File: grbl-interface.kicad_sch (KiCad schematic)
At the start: 12 parts, among them U6 USBLC6-2SC6, U7 ADUM4160, U8 ATmega16U2-A, U9 ATmega328P-A, Y1 Crystal_GND24

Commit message: GRBL PCB controller work
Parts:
- removed D10, D9: Znr, symbol Device:D_Zener
- removed D8: D_Zener, symbol Device:D_Zener
- added C13, C14: 22p, Capacitor_SMD:C_0402_1005Metric_Pad0.74x0.62mm_HandSolder, symbol Device:C
- added C15: 1u, Capacitor_SMD:C_0603_1608Metric, symbol Device:C
- added C16, C18, C19, C20, C21, C24, C25, C26: 100n, Capacitor_SMD:C_0603_1608Metric, symbol Device:C
- added C27: 22u TANT, Capacitor_SMD:C_1206_3216Metric, symbol Device:C_Polarized_US
- added C28: TBD_SPACER (DNI), symbol Device:C
- added D10, D9: YELLOW, -Project:LED_0402_DOT, symbol Device:LED
- added D11, D8: CD1206-S01575, -Project:D_SOD-523_DOT, symbol Device:D
- added F1: TBU-CA065-500-WH, Fuse:Fuse_Bourns_TBU-CA, symbol Power_Protection:TBU-CA065-500-WH
- added J21: USB_B_Mini, Connector_USB:USB_Mini-B_Wuerth_65100516121_Horizontal, symbol Connector:USB_B_Mini
- added J22: uISP, -Project:ISP_SMD_100mil, symbol Connector_Generic:Conn_02x03_Odd_Even
- added J23: ISP, -Project:ISP_SMD_100mil, symbol Connector_Generic:Conn_02x03_Odd_Even
- added L2: CG0603MLC-05E, symbol Device:L
- added L3: 10uH, symbol Device:L
- added R21: 1M, symbol Device:R
- added R23, R30: 10K, symbol Device:R
- added R25, R26, R27, R28, R29: 1K, symbol Device:R
- added SW3: RESET, symbol Switch:SW_Push
- added Y1: 16MHz, symbol Device:Crystal_GND24
- C17: renamed from C13; value C -> 100n; footprint (none) -> Capacitor_SMD:C_0603_1608Metric
- C22: renamed from C14; value C -> 22p; footprint (none) -> Capacitor_SMD:C_0402_1005Metric_Pad0.74x0.62mm_HandSolder
- C23: renamed from C15; value C -> 22p; footprint (none) -> Capacitor_SMD:C_0402_1005Metric_Pad0.74x0.62mm_HandSolder
- U9: value ATmega328P-A -> ATmega328P-AU
- Y2: renamed from Y1; value Crystal_GND24 -> CSTCE16M0V53-R0 16MHZ
- renumbered R21 to R24, U8 to U7, U7 to U8
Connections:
- net GND3 is gone; now on net uGND: C17.2, R24.1, U8.2 (GND1), U8.8 (GND1)
- net +5VA: now also U7.31 (UVCC), U7.32 (AVCC), U7.4 (VCC), U8.12 (PIN), U8.13 (SPD), U8.14 (VDD2), C16.2, C21.2, C24.2, C25.2, C27.1, D11.1 (K), D8.1 (K), J22.2 (Pin_2), J23.2 (Pin_2), L3.1, R23.1, R28.1, R29.1, R30.1; no longer U9.18 (AVCC)
- net GND1: no longer U9.21 (GND), U9.3 (GND), U9.5 (GND), Y2.4
- net P12_IN: now also J23.1 (Pin_1)
- net P16_OUT: now also J23.3 (Pin_3)
- net P17_OUT: now also J23.4 (Pin_4)
- net RX: now also R27.1
- net TX: now also R26.1
- net uD-: now reaches U6.1 (I/O1)
- net uD-: now also J21.2 (D-)
- net uGND: now reaches U6.2 (GND)
- net uGND: now also C18.1, J21.5 (GND), L2.2
- net uD+: now reaches U6.3 (I/O2)
- net uD+: now also J21.3 (D+)
- net at U6.4 (I/O2): now also U8.7 (UD+)
- net at U6.5 (VBUS): now also C17.1, R24.2, U8.3 (VDD1), U8.4 (PDEN), U8.5 (SPU), F1.3
- net at U6.6 (I/O1): now also U8.6 (UD-)
- net RESET: now reaches U9.29 (~{RESET}/PC6)
- net RESET: now also C20.2, D11.2 (A), J23.5 (Pin_5), R30.2, SW3.2
- net at U7.1 (XTAL1): now also C13.1, R21.2, Y1.1
- net RX_LED: now reaches U7.10 (PD4)
- net RX_LED: now also D9.1 (K)
- net TX_LED: now reaches U7.11 (PD5)
- net TX_LED: now also D10.1 (K)
- net DTR: now reaches U7.13 (~{HWB}/PD7)
- net DTR: now also C20.1, R25.1
- net uSCK: now reaches U7.15 (PB1)
- net uSCK: now also J22.3 (Pin_3)
- net uMOSI: now reaches U7.16 (PB2)
- net uMOSI: now also J22.4 (Pin_4)
- net uMISO: now reaches U7.17 (PB3)
- net uMISO: now also J22.1 (Pin_1)
- net at U7.2 (PC0/XTAL2): now also C14.2, R21.1, Y1.3
- net uRESET: now reaches U7.24 (PC1/~{RESET})
- net uRESET: now also D8.2 (A), J22.5 (Pin_5), R23.2
- net at U7.27 (UCAP): now also C15.1
- net GND: now reaches U7.28 (UGND)
- net GND: now also U7.3 (GND), U8.15 (GND2), U8.9 (GND2), U9.21 (GND), U9.3 (GND), U9.5 (GND), Y2.4, C13.2, C14.1, C15.2, C16.1, C19.1, C21.1, C24.1, C25.1, C26.1, C27.2, J22.6 (Pin_6), J23.6 (Pin_6), R25.2, SW3.1, Y1.2, Y1.4
- net D+: now reaches U7.29 (D+)
- net D+: now also U8.10 (DD+)
- net D-: now reaches U7.30 (D-)
- net D-: now also U8.11 (DD-)
- net uRX: now reaches U7.8 (PD2)
- net uRX: now also R26.2
- net uTX: now reaches U7.9 (PD3)
- net uTX: now also R27.2
- net at U8.1 (VBUS1): now also C18.2, C28.2
- net at U8.16 (VBUS2): now also C19.2, C28.1
- new net: C26.2, L3.2, U9.18 (AVCC)
- new net: D9.2 (A), R28.2
- new net: J21.SH (Shield), L2.1
- new net: D10.2 (A), R29.2
- new net VBUS: F1.1, J21.1 (VBUS)
- no-connect marks 3 -> 19
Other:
- moved on the sheet: C17, C22, C23, R24, U6, U7, U8, U9, Y2

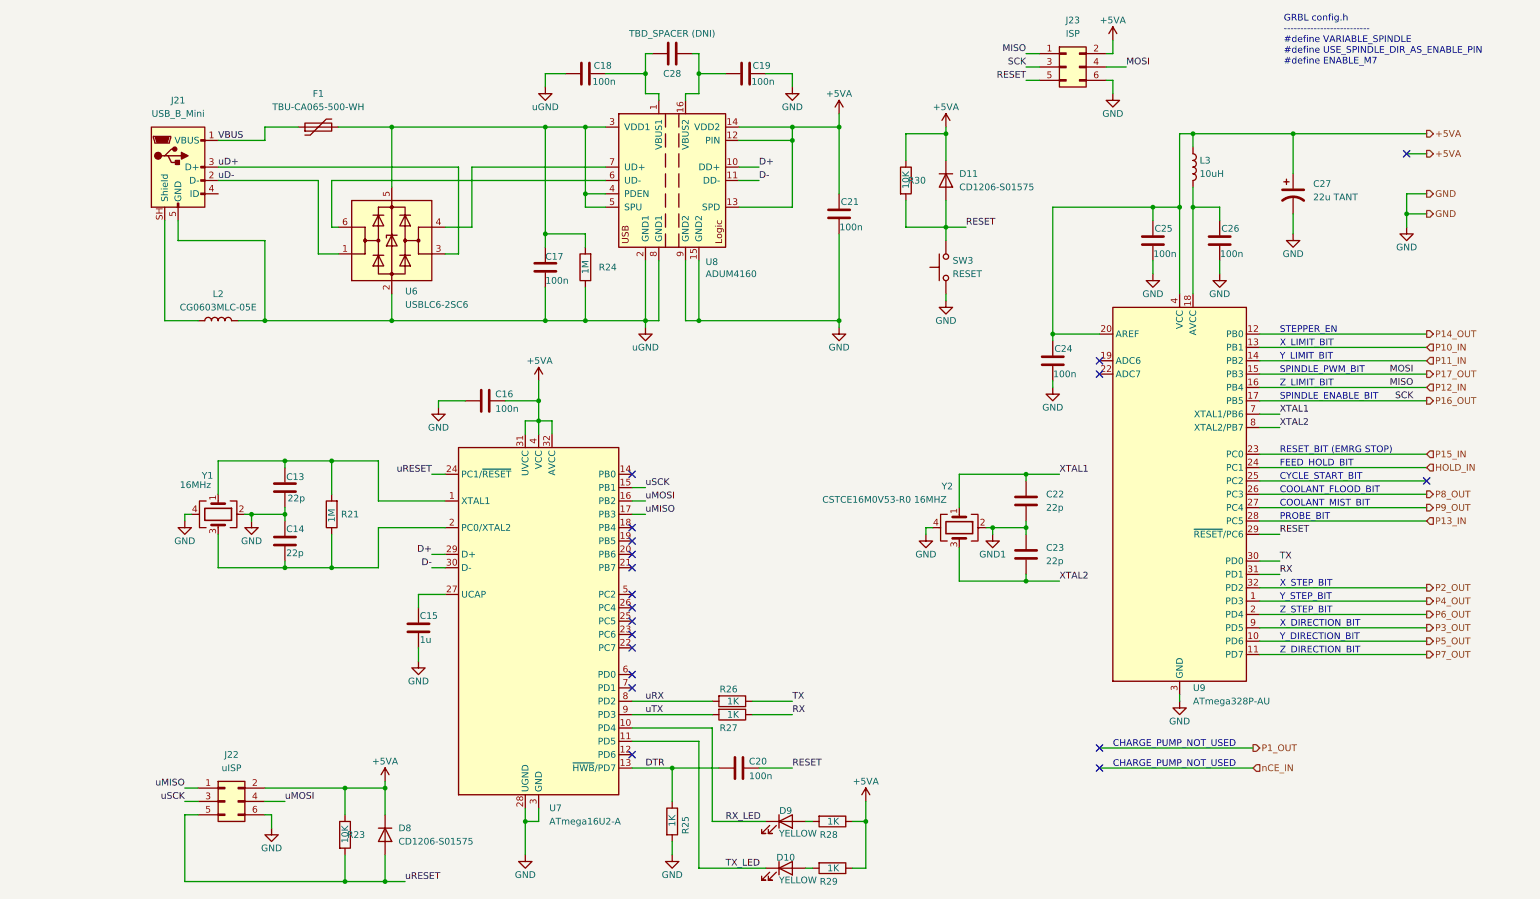
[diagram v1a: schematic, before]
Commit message: v3.3 GRBL Controller WIP
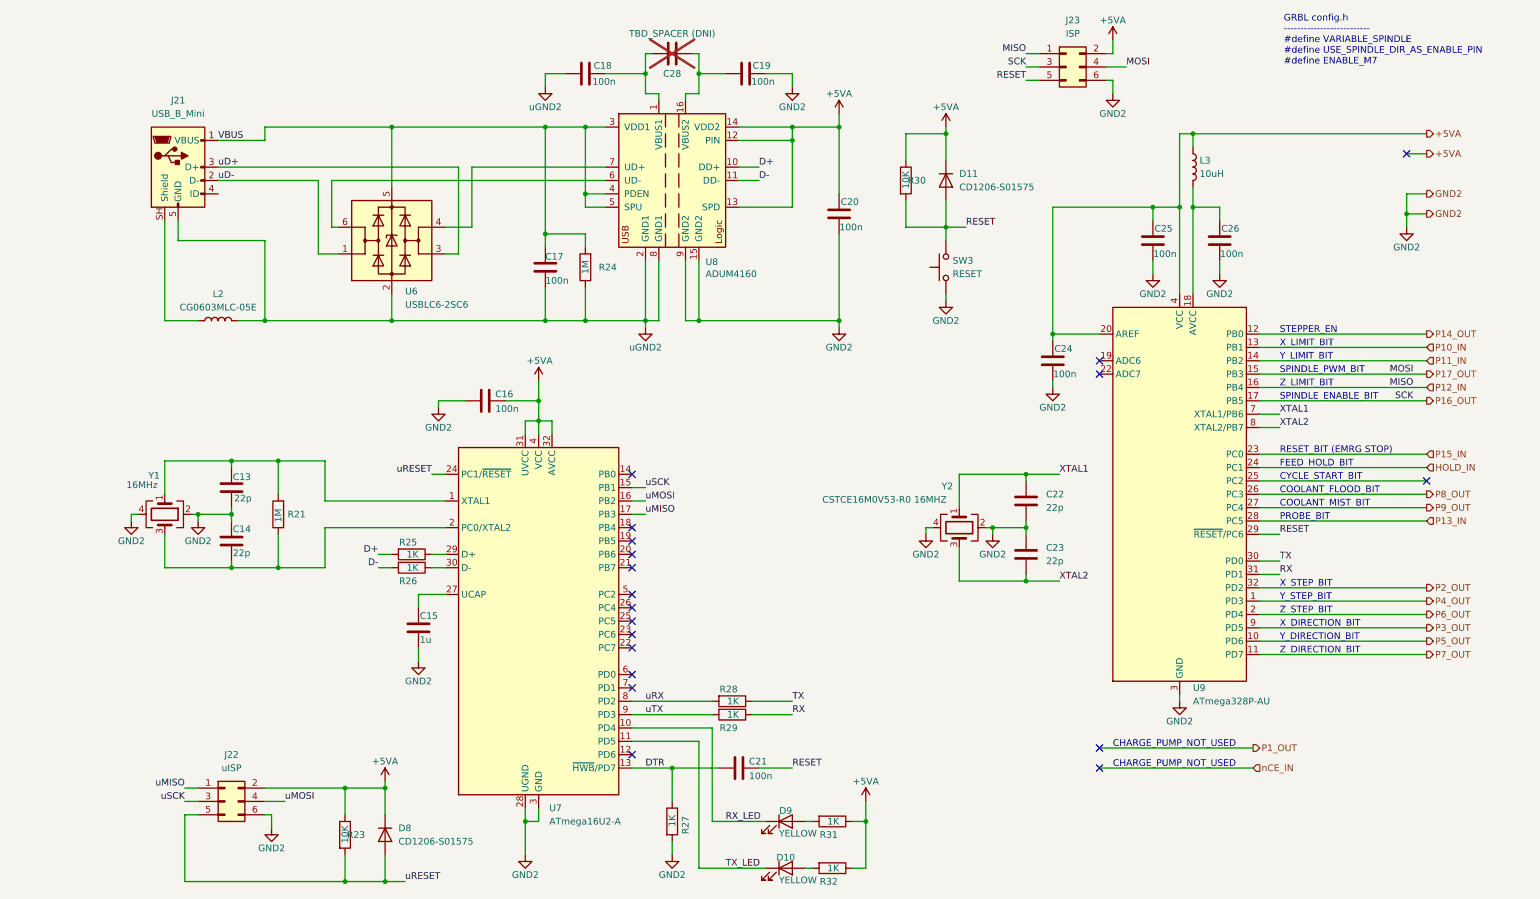
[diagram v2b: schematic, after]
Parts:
- removed C27: 22u TANT, Capacitor_SMD:C_1206_3216Metric, symbol Device:C_Polarized_US
- removed F1: TBU-CA065-500-WH, Fuse:Fuse_Bourns_TBU-CA, symbol Power_Protection:TBU-CA065-500-WH
- added R25, R26: 1K, Resistor_SMD:R_0402_1005Metric_Pad0.72x0.64mm_HandSolder, symbol Device:R
- C17, C18, C19: footprint Capacitor_SMD:C_0603_1608Metric -> Capacitor_SMD:C_0402_1005Metric_Pad0.74x0.62mm_HandSolder
- C20: renamed from C21; footprint Capacitor_SMD:C_0603_1608Metric -> Capacitor_SMD:C_0402_1005Metric_Pad0.74x0.62mm_HandSolder
- C21: renamed from C20; footprint Capacitor_SMD:C_0603_1608Metric -> Capacitor_SMD:C_0402_1005Metric_Pad0.74x0.62mm_HandSolder
- C28: now not fitted; now left out of the parts list
- L2: footprint (none) -> Resistor_SMD:R_0805_2012Metric_Pad1.20x1.40mm_HandSolder
- R21, R23, R24, R30: footprint (none) -> Resistor_SMD:R_0402_1005Metric_Pad0.72x0.64mm_HandSolder
- R27: renamed from R25; footprint (none) -> Resistor_SMD:R_0402_1005Metric_Pad0.72x0.64mm_HandSolder
- R28: renamed from R26; footprint (none) -> Resistor_SMD:R_0402_1005Metric_Pad0.72x0.64mm_HandSolder
- R29: renamed from R27; footprint (none) -> Resistor_SMD:R_0402_1005Metric_Pad0.72x0.64mm_HandSolder
- R31: renamed from R28; footprint (none) -> Resistor_SMD:R_0402_1005Metric_Pad0.72x0.64mm_HandSolder
- R32: renamed from R29; footprint (none) -> Resistor_SMD:R_0402_1005Metric_Pad0.72x0.64mm_HandSolder
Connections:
- net GND1 is gone; now on net GND2: C22.2, C23.1, Y2.2
- net D+: now also R25.2; no longer U7.29 (D+)
- net D-: now also R26.2; no longer U7.30 (D-)
- net VBUS: now also C17.1, R24.2, U6.5 (VBUS), U8.3 (VDD1), U8.4 (PDEN), U8.5 (SPU)
- net GND renamed GND2
- net uGND renamed uGND2
- new net: R26.1, U7.30 (D-)
- new net: R25.1, U7.29 (D+)
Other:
- moved on the sheet: C13, C14, R21, Y1

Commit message: v3.3 GRBL WIP
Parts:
- Y1: value 16MHz -> Crystal_SMD_WE_CFPX-104-4Pin_5.0x3.2mm; footprint (none) -> Crystal:Crystal_SMD_WE_CFPX-104-4Pin_5.0x3.2mm; KiLib_Generator (none) -> crystal_resonator_oscillator
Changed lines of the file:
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@@
 			)
 		)
-		(property "Value" "16MHz"
+		(property "Value" "Crystal_SMD_WE_CFPX-104-4Pin_5.0x3.2mm"
 			(at 21.082 108.712 90)
 			(show_name no)
@@
 			)
 		)
-		(property "Footprint" ""
+		(property "Footprint" "Crystal:Crystal_SMD_WE_CFPX-104-4Pin_5.0x3.2mm"
 			(at 25.4 114.3 0)
 			(hide yes)
@@
 			(show_name no)
 			(do_not_autoplace no)
+			(effects
+				(font
+					(size 1.27 1.27)
+				)
+			)
+		)
+		(property "KiLib_Generator" "crystal_resonator_oscillator"
+			(at 25.4 114.3 0)
+			(hide yes)
+			(show_name no)
+			(do_not_autoplace no)
